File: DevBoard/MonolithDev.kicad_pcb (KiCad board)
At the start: 4 copper layers, 196 x 115 mm, 358 parts, among them J101 Pack (welded 4S) - use instea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, J102 Cell 1 NTC 10k 103AT, J103 EV2400 SMBus, J104 Bench PACK_P, J105 Cell 2 NTC 10k 103AT, J106 Cell 3 NTC 10k 103AT, J107 Cell 4 NTC 10k 103AT, J201 SMA OUT_LO, J202 SMA OUT_HI, J301 SWD, J302 UART debug, J303 Spare GPIO, J401 TYPE-C 16PCB0.8 IP68, J402 I2CC logic analyzer, J501 TYPE-C 16PCB0.8 IP68, J502 I2CC logic analyzer, Q101 AGM404AP1, Q102 AGM404AP1, Q103 BSS138, Q401 IAUC45N04S6L063H, Q402 IAUC45N04S6L063H, Q501 IAUC45N04S6L063H, Q502 IAUC45N04S6L063H, SW101 WAKE, SW301 RESET, U101 BQ40Z50RSMR-R2, U201 INA190A5IDDFR, U202 INA190A1IDDFR, U203 TPS70950DBVR, U204 TPS62177DQCR, U301 STM32WB1MMC, U401 TPS25751DREFR, U402 M24512-DFMC6TG, U403 BQ25756RRVR, U404 TPS62933DRLR, U501 TPS25751DREFR, U502 M24512-DFMC6TG, U503 BQ25756RRVR, U504 TPS62933DRLR

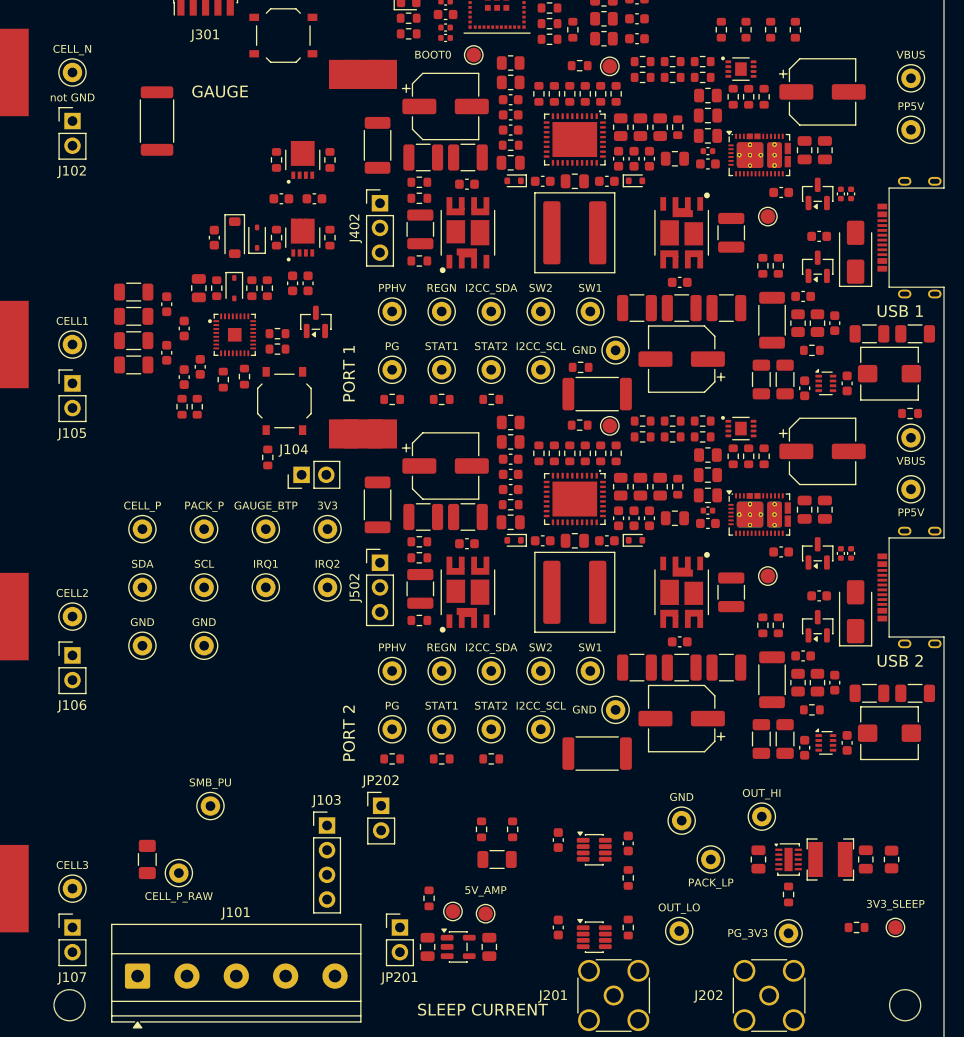
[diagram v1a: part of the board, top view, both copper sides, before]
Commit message: Dev board: SMD test loops (RH-S2761-46R) instead of Keystone through-hole
All 45 loop test points become ronghe RH-S2761-46R (LCSC C55121754), the
JLC-stocked equivalent of the Harwin S2761-46R: 1.6 x 0.8 x 1.15 mm SMT
loop on an 0603 land pattern, 3.5 A. New footprint
MonolithDev:TestPoint_Harwin_S2761_0603 (make_footprints.py section 11),
both pads pin 1 and jumpered. JLC places them; no through-hole assembly.

Co-Authored-By: Claude Opus 5.5 <noreply@anthropic.com>
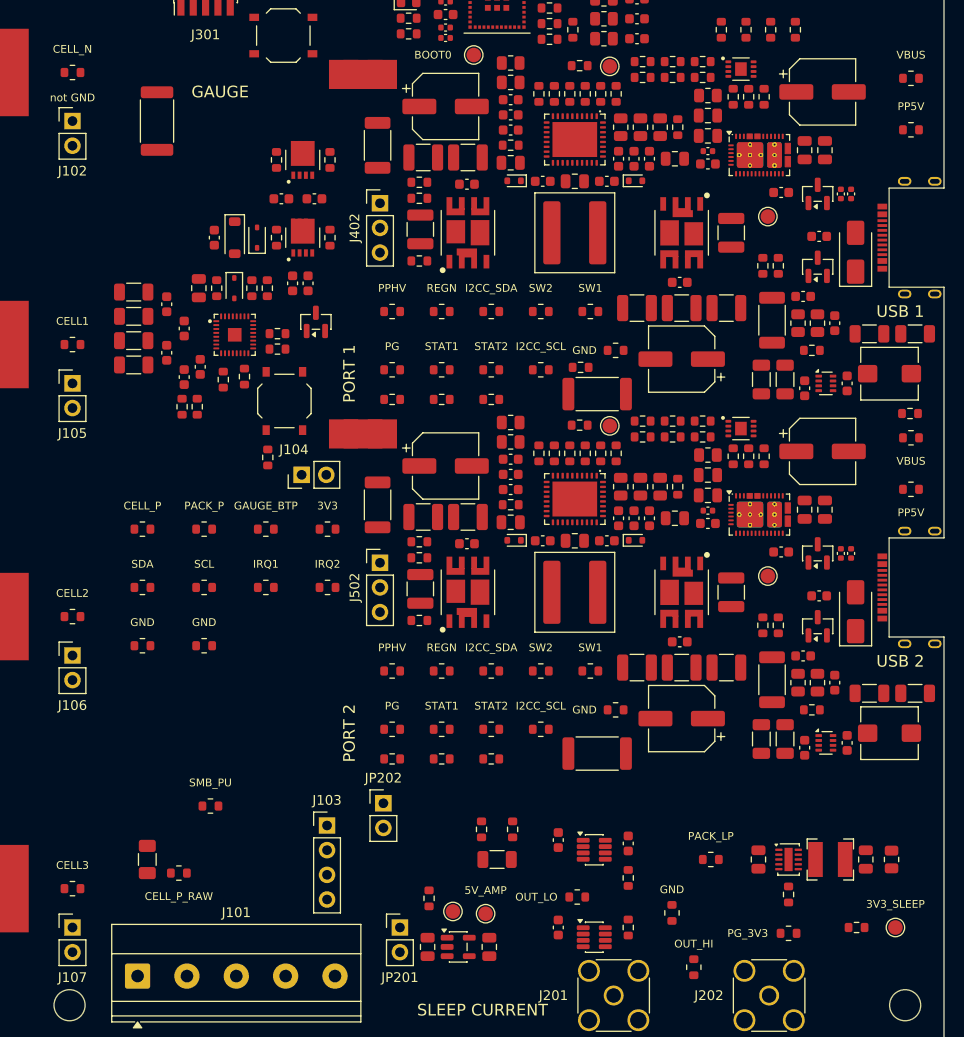
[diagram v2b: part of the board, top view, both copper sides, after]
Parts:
- TP101, TP102, TP103, TP104, TP105, TP106, TP107, TP108, TP109, TP201, TP202, TP203, TP204, TP205, TP301, TP302, TP303, TP304, TP305, TP308, TP309, TP401, TP402, TP403, TP404, TP405, TP406, TP407, TP408, TP409, TP410, TP411, TP412, TP501, TP502, TP503, TP504, TP505, TP506, TP507, TP508, TP509, TP510, TP511, TP512: footprint TestPoint:TestPoint_Keystone_5000-5004_Miniature -> MonolithDev:TestPoint_Harwin_S2761_0603
- moved TP202 17.0 mm to (220.2, 157.1), turned to 90 degrees
- moved TP201 11.1 mm to (208.2, 149.9)
- moved TP203 9.55 mm to (218.0, 151.5), turned to 90 degrees
- moved JP202 0.35 mm to (188.3, 140.2)

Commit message: Dev board: open-item pass, J104 diode, antenna keep-out, bring-up checklist
- D104 SS34 in series with the J104 bench input (reversed lead, back-feed).
- ANT_KEEPOUT rule area (no tracks/vias/pours, all copper layers) around
  the STM32WB1MMC antenna end, created by place_parts.py.
- D401 drawn unidirectional; header part numbers (PZ254V-11 family);
  shunt, J301 keying, B-constant, insulated-NTC, sheet-text and R201 notes.
- docs/devboard/bringup-config-checklist.md: every configuration item from
  both reviews in bring-up order, with review 2's precharge correction;
  review 1's 0 mV precharge line marked superseded.

Co-Authored-By: Claude Opus 5.5 <noreply@anthropic.com>
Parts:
- added D104: SS34, Diode_SMD:D_SMA, F.Cu at (171.9, 106.4)
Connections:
- J104 pad 1: PACK_P -> Net-(D104-A)

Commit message: Dev board: TH305 at the protection FETs; drop the gauge-BAT INA190 idea
- TH305 (10k NTC) between Q101/Q102 on PA7 / ADC1_IN2, same 10k 1 % /
  0.1 uF divider from NTC_EN (R320, C312). PA7 net renamed NTC_TH5, still
  on J303 pin 2. Placed beside C111; R320/C312 under J303.
- Optional third INA190 on the gauge BAT feed dropped: measure the gauge
  supply as the drop across R105 (100 R, 50-340 uA = 5-34 mV).

Co-Authored-By: Claude Opus 5.5 <noreply@anthropic.com>
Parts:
- added C312: 0.1u 50V, Capacitor_SMD:C_0603_1608Metric, F.Cu at (220.2, 60.6)
- added R320: 10k 1%, Resistor_SMD:R_0805_2012Metric, F.Cu at (218.0, 60.6)
- added TH305: 10k B3435, Resistor_SMD:R_0603_1608Metric, F.Cu at (183.6, 77.8)
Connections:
- net /MCU and NTCs/PA7 renamed /MCU and NTCs/NTC_TH5

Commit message: Dev board: holder tab hole, Samtec J301 land pattern, 3D models, measured USB-C STEP
- Cell holder footprint: add the dia 2.25 hole for the + terminal locating
  tab (from the rendered MYOUNG drawing; the holder could not seat flat).
- J301 on Samtec's recommended FTSH-1xx-DV land pattern with the -K shroud
  courtyard; J301 and the MCU title moved to fit.
- 3D models on 292 of 362 footprints: custom footprints borrow same-body
  KiCad models (pin 1 checked in renders); SMA and TS-1187A re-pointed to
  shipped models by place_parts.py.
- USB-C (J401/J501): STEP model measured from ShouHan's vector drawing
  (tools/drawing_extract, tools/make_3d_usbc.py) and verified by hidden-line
  overlays on all three views (3dmodels/verification).
- Placer: test-point labels sorted by reference; hidden only when no spot.
- docs/devboard/power-budget.md; renders in DevBoard/renders.

Co-Authored-By: Claude Opus 5.5 <noreply@anthropic.com>
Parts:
- J301: footprint Connector_PinHeader_1.27mm:PinHeader_2x05_P1.27mm_Vertical_SMD -> MonolithDev:Samtec_FTSH-105-01-xx-DV-K_2x05_P1.27mm
- moved J301 1.20 mm to (168.8, 56.0)

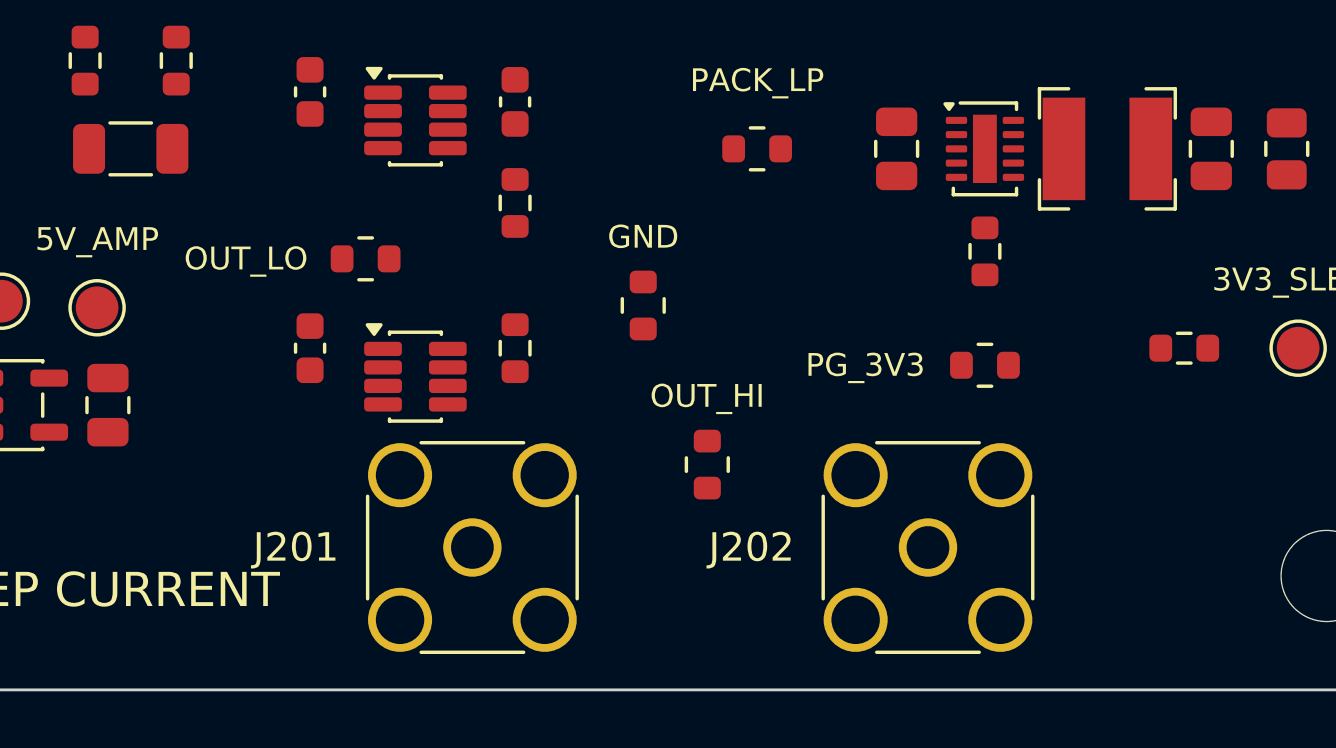
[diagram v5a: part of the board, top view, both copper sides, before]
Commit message: Dev board: 3D models for every physical part; holder, cell, module, renders
- Cell holders: LCSC EasyEDA model corrected against MYOUNG's drawing
  (side walls clipped/filled to the drawn profile, logo removed, + tab
  added); hidden-line overlays in 3dmodels/verification match both views.
- EVE INR21700/58E cell as a second model on the holder footprint; axis
  height 13.18 is PROVISIONAL (not in MYOUNG's drawing) - measure.
- STM32WB1MMC: LCSC EasyEDA model checked against ST fig. 11 / table 3
  (6.5 x 10 x 1.372, pad pattern and pin A1 match the footprint).
- M24512 UFDFPN8 and the S2761 test loop from their package drawings.
- 346 of 362 footprints modelled (rest: holes, bare pads, net ties).
- Fresh renders: top, iso front/rear, holders, USB-C, MCU, side, bottom.

Co-Authored-By: Claude Opus 5.5 <noreply@anthropic.com>
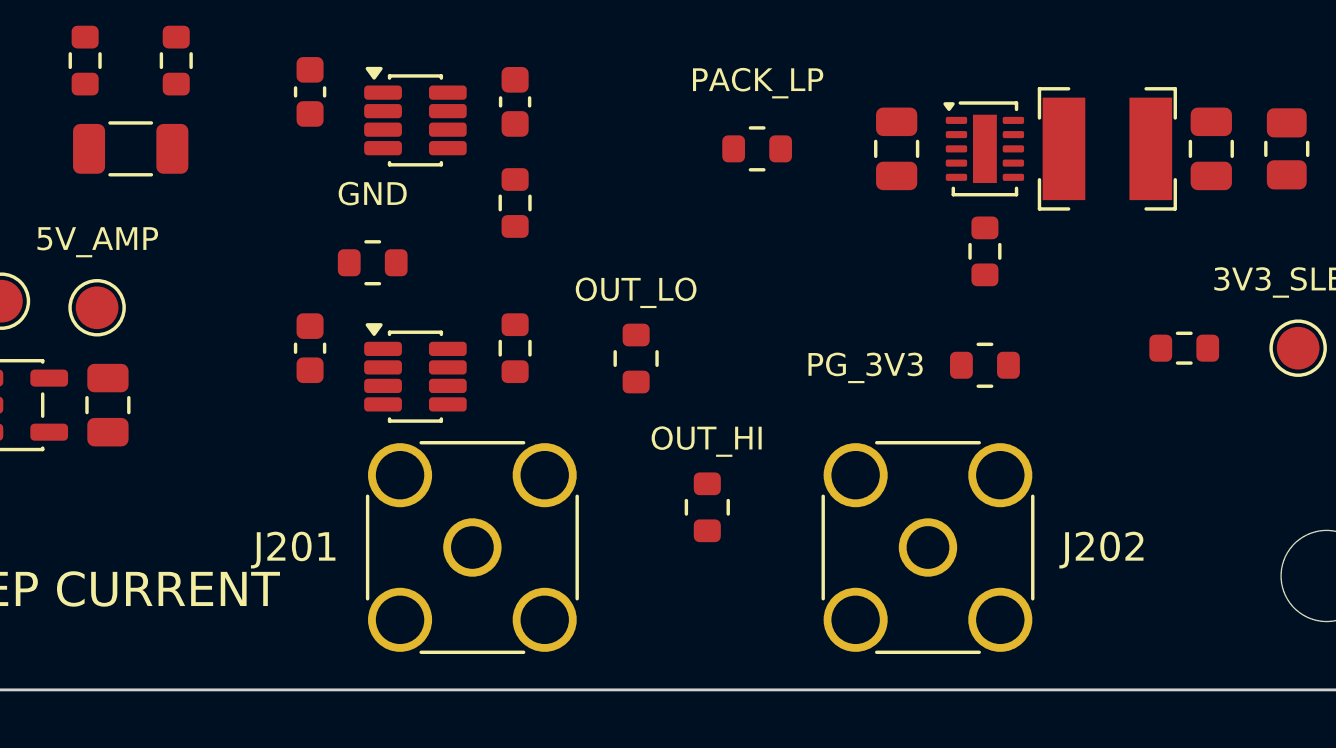
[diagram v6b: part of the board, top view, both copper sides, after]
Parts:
- moved TP201 10.1 mm to (217.8, 153.4), turned to 90 degrees
- moved TP203 9.62 mm to (208.5, 150.0), turned to 0 degrees
- moved TP202 1.50 mm to (220.2, 158.6)

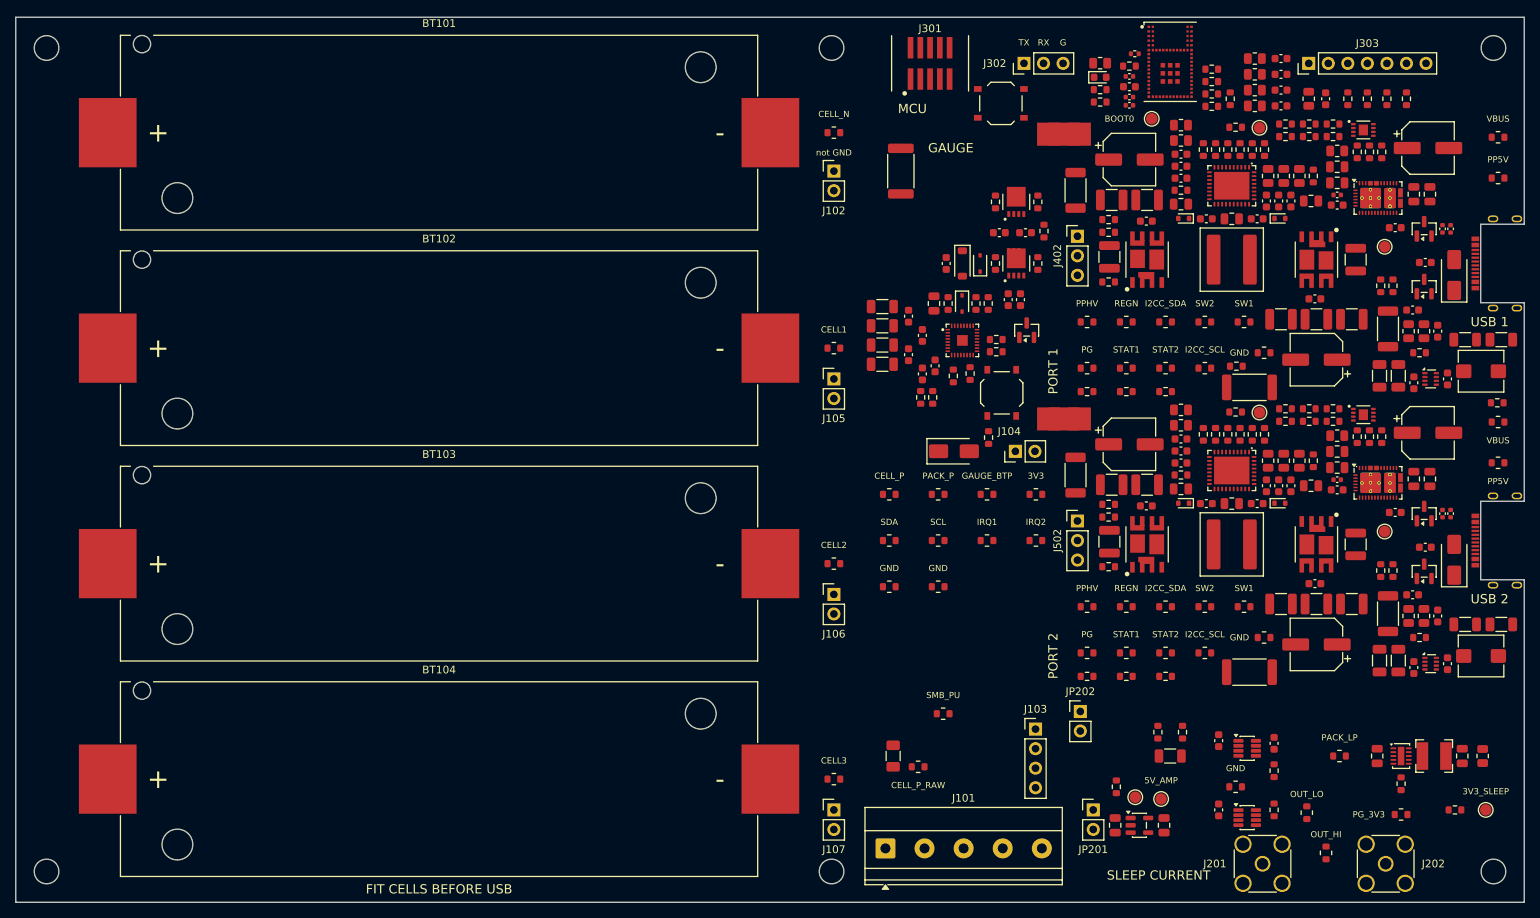
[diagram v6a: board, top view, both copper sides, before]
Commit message: Dev board: silkscreen purpose/pinout labels; sleep-current SMAs to test loops
- Silkscreen: WAKE / RESET / AMP EN / MEAS PWR / SWD part labels and pin
  labels on J101, J102-J107, J103, J104, J303, J402/J502, J301 pin 1
  (place_parts.py PIN_LABELS / PART_LABELS; README item 30).
- J201/J202 vertical SMAs removed: OUT_LO/OUT_HI probed on TP201/TP202, each
  with a GND loop (TP208/TP209) 4.5 mm away, in a row on the bottom edge.
  R204/R205 49.9R kept (README item 31; docs updated).
- Renders, 2D exports and schematic PDF regenerated.

Co-Authored-By: Claude Opus 5.5 <noreply@anthropic.com>
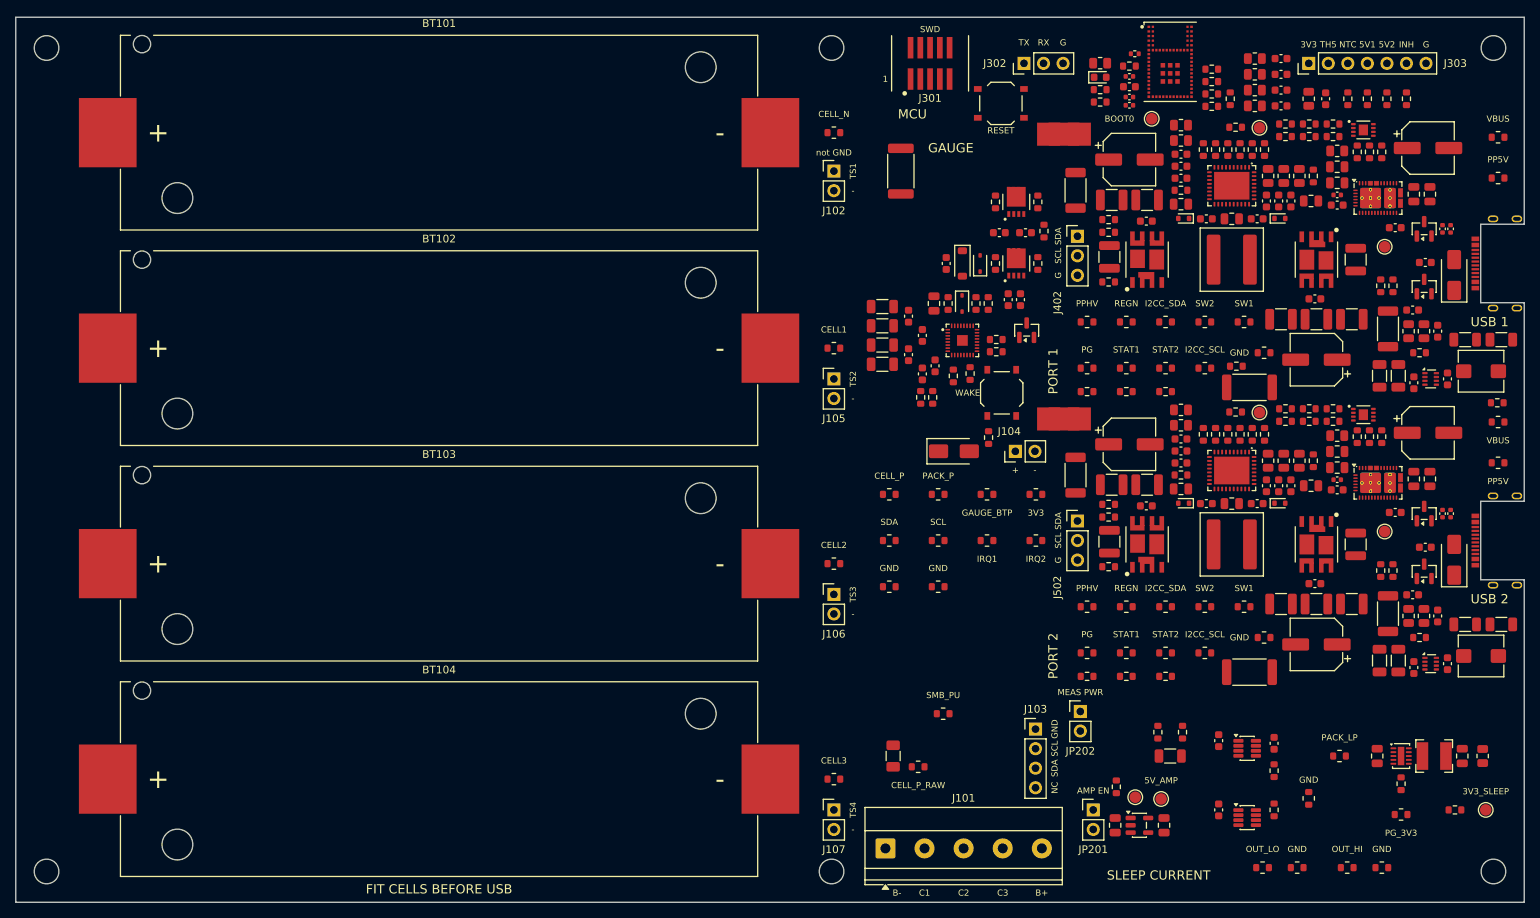
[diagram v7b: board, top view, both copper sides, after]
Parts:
- removed J201: SMA OUT_LO, Connector_Coaxial:SMA_Amphenol_132134_Vertical
- removed J202: SMA OUT_HI, Connector_Coaxial:SMA_Amphenol_132134_Vertical
- added TP208: GND, MonolithDev:TestPoint_Harwin_S2761_0603, F.Cu at (216.5, 160.5)
- added TP209: GND, MonolithDev:TestPoint_Harwin_S2761_0603, F.Cu at (227.5, 160.5)
- moved TP203 9.62 mm to (218.0, 151.5), turned to 90 degrees
- moved TP201 9.17 mm to (212.0, 160.5), turned to 0 degrees
- moved TP202 3.35 mm to (223.0, 160.5), turned to 0 degrees
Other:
- board text added: "+"
- board text added: "-"
- board text added: "1"
- board text added: "3V3"
- board text added: "5V1"
- board text added: "5V2"
- board text added: "AMP EN"
- board text added: "B+"
- board text added: "B-"
- board text added: "C1"
- board text added: "C2"
- board text added: "C3"
- board text added: "GND"
- board text added: "INH"
- board text added: "MEAS PWR"
- board text added: "NC"
- board text added: "NTC"
- board text added: "RESET"
- board text added: "SCL"
- board text added: "SDA"
- board text added: "SWD"
- board text added: "TH5"
- board text added: "TS1"
- board text added: "TS2"
- board text added: "TS3"
- board text added: "TS4"
- board text added: "WAKE"
